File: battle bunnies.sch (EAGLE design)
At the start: 79 parts, among them IC1 CP2104, Q1 mmbt2222, Q2 mmbt2222, SW2 KMR2, U1 PCA9685, U2 SPX3819, U3 MCP73831T-2ACI/OT, X2 ESP-12, X4 20329

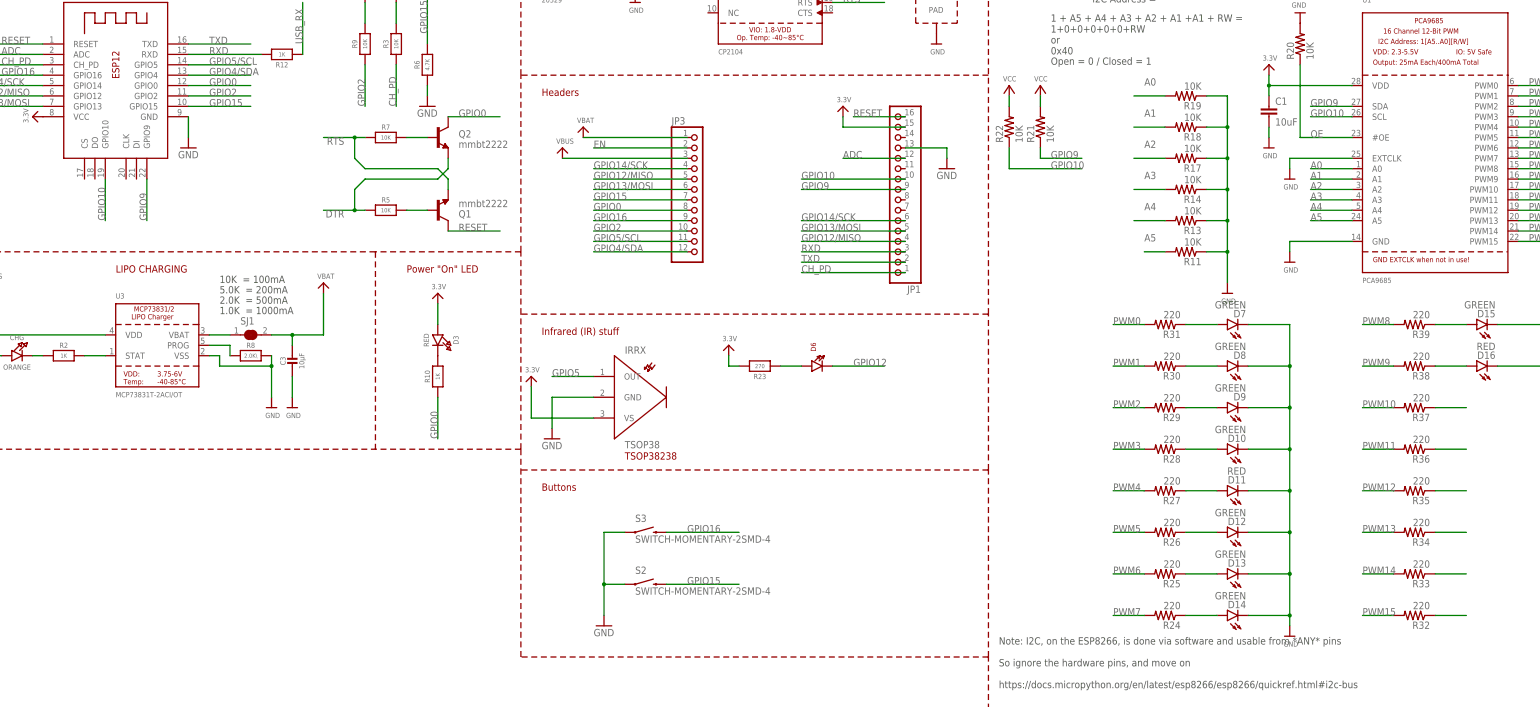
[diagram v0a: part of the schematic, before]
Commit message: Updating schematic, and initial layout
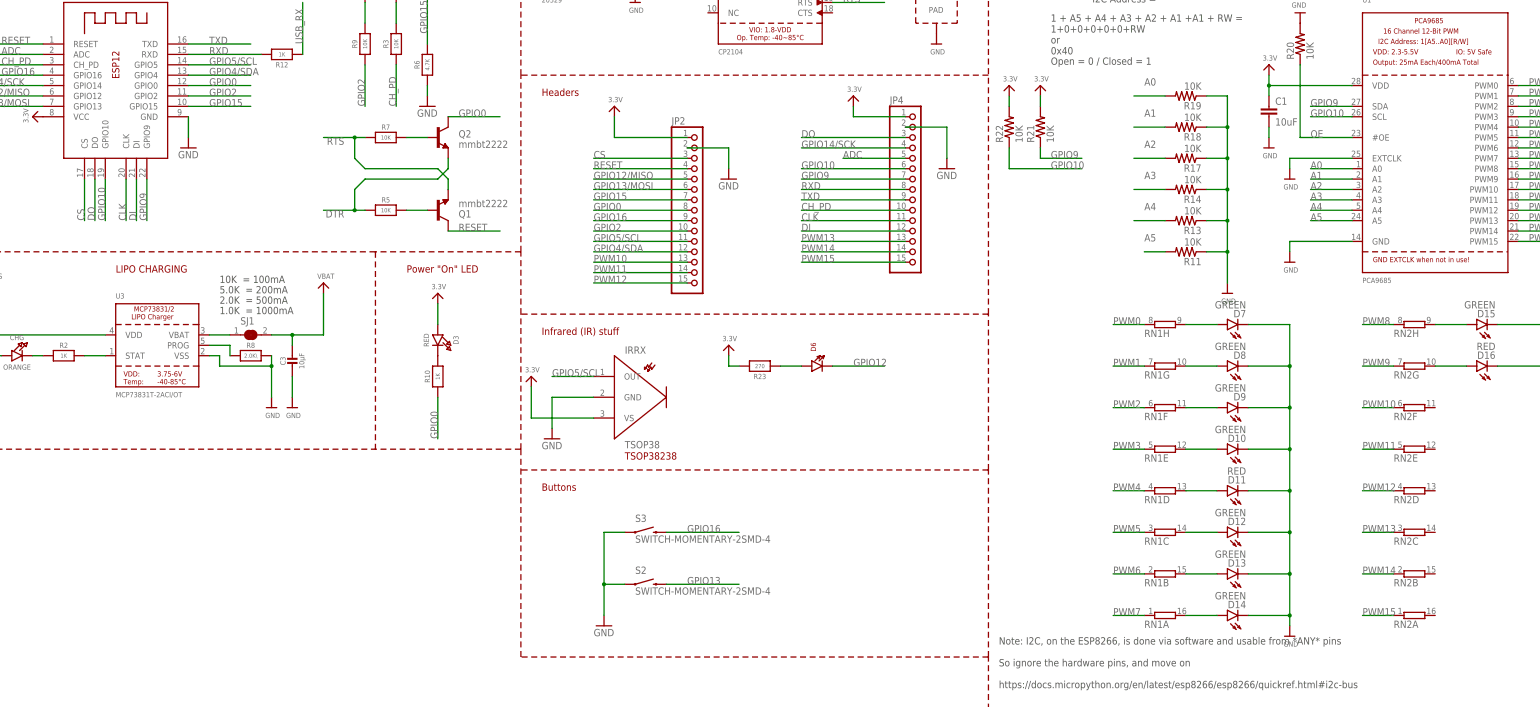
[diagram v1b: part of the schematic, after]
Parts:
- removed JP1: (no value), microbuilder:HEADER-1X16ROUND
- removed JP3: (no value), microbuilder:HEADER-1X12
- removed R24, R25, R26, R27, R28, R29, R30, R31, R32, R33, R34, R35, R36, R37, R38, R39: 220, SparkFun-Passives:RESISTOR0805-RES
- added JP2, JP4: (no value), pinhead:PINHD-1X15
- added RN1, RN2: (no value), resistor-dil:8R-NEXB2HV
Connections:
- removed net GPIO5: IRRX.OUT
- removed net N$25: R37.1
- removed net N$26: R36.1
- removed net N$27: R35.1
- removed net N$28: R34.1
- removed net N$29: R33.1
- removed net N$30: R32.1
- removed net VCC: R21.2, R22.2
- new net CLK: JP4.11, X2.CLK
- new net CS: JP2.3, X2.CS
- new net DI: JP4.12, X2.DI
- new net DO: JP4.3, X2.DO
- new net GPIO13: S2.2
- net 3.3V: now also JP2.1, JP4.1, R21.2, R22.2; no longer JP1.15
- net ADC: now also JP4.5; no longer JP1.12
- net CH_PD: now also JP4.10; no longer JP1.1
- net EN: no longer JP3.2
- net GND: now also JP2.2, JP4.2; no longer JP1.13
- net GPIO0: now also JP2.8; no longer JP3.8
- net GPIO10: now also JP4.6; no longer JP1.10
- net GPIO12/MISO: now also JP2.5; no longer JP1.4, JP3.5
- net GPIO13/MOSI: now also JP2.6; no longer JP1.5, JP3.6
- net GPIO14/SCK: now also JP4.4; no longer JP1.6, JP3.4
- net GPIO15: now also JP2.7; no longer JP3.7, S2.2
- net GPIO16: now also JP2.9; no longer JP3.9
- net GPIO2: now also JP2.10; no longer JP3.10
- net GPIO4/SDA: now also JP2.12; no longer JP3.12
- net GPIO5/SCL: now also IRRX.OUT, JP2.11; no longer JP3.11
- net GPIO9: now also JP4.7; no longer JP1.9
- net N$15: now also RN1B.2; no longer R25.1
- net N$16: now also RN1A.2; no longer R24.1
- net N$17: now also RN1C.2; no longer R26.1
- net N$18: now also RN1D.2; no longer R27.1
- net N$19: now also RN1E.2; no longer R28.1
- net N$20: now also RN1F.2; no longer R29.1
- net N$21: now also RN1G.2; no longer R30.1
- net N$22: now also RN1H.2; no longer R31.1
- net N$23: now also RN2H.2; no longer R39.1
- net N$24: now also RN2G.2; no longer R38.1
- net PWM0: now also RN1H.1; no longer R31.2
- net PWM1: now also RN1G.1; no longer R30.2
- net PWM10: now also JP2.13, RN2F.1; no longer R37.2
- net PWM11: now also JP2.14, RN2E.1; no longer R36.2
- net PWM12: now also JP2.15, RN2D.1; no longer R35.2
- net PWM13: now also JP4.13, RN2C.1; no longer R34.2
- net PWM14: now also JP4.14, RN2B.1; no longer R33.2
- net PWM15: now also JP4.15, RN2A.1; no longer R32.2
- net PWM2: now also RN1F.1; no longer R29.2
- net PWM3: now also RN1E.1; no longer R28.2
- net PWM4: now also RN1D.1; no longer R27.2
- net PWM5: now also RN1C.1; no longer R26.2
- net PWM6: now also RN1B.1; no longer R25.2
- net PWM7: now also RN1A.1; no longer R24.2
- net PWM8: now also RN2H.1; no longer R39.2
- net PWM9: now also RN2G.1; no longer R38.2
- net RESET: now also JP2.4; no longer JP1.16
- net RXD: now also JP4.8; no longer JP1.3
- net TXD: now also JP4.9; no longer JP1.2
- net VBAT: no longer JP3.1
- net VBUS: no longer JP3.3

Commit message: Updating with latest routing attempt
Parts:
- removed R11, R13, R14, R17, R18, R19: 10K, SparkFun-Passives:RESISTOR0805-RES
- added RN3: (no value), resistor-dil:8R-NEXB2HV
- RN1: value (none) -> 220
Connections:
- removed net GPIO13: S2.2
- net A0: now also RN3E.1; no longer R19.2
- net A1: now also RN3D.1; no longer R18.2
- net A2: now also RN3C.1; no longer R17.2
- net A3: now also RN3B.1; no longer R14.2
- net A4: now also RN3A.1; no longer R13.2
- net A5: now also RN3F.1; no longer R11.2
- net GND: now also RN3A.2, RN3B.2, RN3C.2, RN3D.2, RN3E.2, RN3F.2; no longer R11.1, R13.1, R14.1, R17.1, R18.1, R19.1
- net GPIO13/MOSI: now also S2.2
- net PWM10: no longer RN2F.1
- net PWM11: no longer RN2E.1
- net PWM12: no longer RN2D.1
- net PWM13: no longer RN2C.1
- net PWM14: no longer RN2B.1
- net PWM15: no longer RN2A.1
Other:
- moved on the sheet: RN2A, RN2B, RN2C, RN2D, RN2E, RN2F
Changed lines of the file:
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@@
 <?xml version="1.0" encoding="utf-8"?>
 <!DOCTYPE eagle SYSTEM "eagle.dtd">
-<eagle version="7.7.0">
+<eagle version="7.6.0">
 <drawing>
 <settings>
@@
 <part name="U$63" library="microbuilder" deviceset="GND" device=""/>
 <part name="U$69" library="microbuilder" deviceset="GND" device=""/>
-<part name="R11" library="SparkFun-Passives" deviceset="RESISTOR" device="0805-RES" value="10K"/>
-<part name="R13" library="SparkFun-Passives" deviceset="RESISTOR" device="0805-RES" value="10K"/>
-<part name="R14" library="SparkFun-Passives" deviceset="RESISTOR" device="0805-RES" value="10K"/>
-<part name="R17" library="SparkFun-Passives" deviceset="RESISTOR" device="0805-RES" value="10K"/>
-<part name="R18" library="SparkFun-Passives" deviceset="RESISTOR" device="0805-RES" value="10K"/>
-<part name="R19" library="SparkFun-Passives" deviceset="RESISTOR" device="0805-RES" value="10K"/>
 <part name="U$70" library="microbuilder" deviceset="GND" device=""/>
 <part name="C1" library="SparkFun-Capacitors" deviceset="10UF10V10%(0805)" device="" value="10uF"/>
@@
 <part name="U$35" library="microbuilder" deviceset="3.3V" device=""/>
 <part name="GND7" library="supply1" deviceset="GND" device=""/>
+<part name="RN1" library="resistor-dil" deviceset="8R-N" device="EXB2HV" value="220"/>
 <part name="RN2" library="resistor-dil" deviceset="8R-N" device="EXB2HV"/>
-<part name="RN1" library="resistor-dil" deviceset="8R-N" device="EXB2HV"/>
+<part name="RN3" library="resistor-dil" deviceset="8R-N" device="EXB2HV"/>
 </parts>
 <sheets>
@@
 <instance part="U$63" gate="G$1" x="325.12" y="142.24"/>
 <instance part="U$69" gate="G$1" x="309.88" y="134.62"/>
-<instance part="R11" gate="G$1" x="299.72" y="144.78" rot="R180"/>
-<instance part="R13" gate="G$1" x="299.72" y="152.4" rot="R180"/>
-<instance part="R14" gate="G$1" x="299.72" y="160.02" rot="R180"/>
-<instance part="R17" gate="G$1" x="299.72" y="167.64" rot="R180"/>
-<instance part="R18" gate="G$1" x="299.72" y="175.26" rot="R180"/>
-<instance part="R19" gate="G$1" x="299.72" y="182.88" rot="R180"/>
 <instance part="U$70" gate="G$1" x="320.04" y="170.18"/>
 <instance part="C1" gate="G$1" x="320.04" y="177.8"/>
@@
 <instance part="U$35" gate="G$1" x="160.02" y="180.34"/>
 <instance part="GND7" gate="1" x="187.96" y="162.56"/>
-<instance part="RN2" gate="A" x="355.6" y="55.88"/>
-<instance part="RN2" gate="B" x="355.6" y="66.04"/>
-<instance part="RN2" gate="C" x="355.6" y="76.2"/>
-<instance part="RN2" gate="D" x="355.6" y="86.36"/>
-<instance part="RN2" gate="E" x="355.6" y="96.52"/>
-<instance part="RN2" gate="F" x="355.6" y="106.68"/>
-<instance part="RN2" gate="G" x="355.6" y="116.84"/>
-<instance part="RN2" gate="H" x="355.6" y="127"/>
 <instance part="RN1" gate="A" x="294.64" y="55.88"/>
 <instance part="RN1" gate="B" x="294.64" y="66.04"/>
@@
 <instance part="RN1" gate="G" x="294.64" y="116.84"/>
 <instance part="RN1" gate="H" x="294.64" y="127"/>
+<instance part="RN2" gate="A" x="368.3" y="104.14"/>
+<instance part="RN2" gate="B" x="368.3" y="99.06"/>
+<instance part="RN2" gate="C" x="368.3" y="93.98"/>
+<instance part="RN2" gate="D" x="368.3" y="88.9"/>
+<instance part="RN2" gate="E" x="368.3" y="83.82"/>
+<instance part="RN2" gate="F" x="368.3" y="78.74"/>
+<instance part="RN2" gate="G" x="355.6" y="116.84"/>
+<instance part="RN2" gate="H" x="355.6" y="127"/>
+<instance part="RN3" gate="A" x="299.72" y="152.4"/>
+<instance part="RN3" gate="B" x="299.72" y="160.02"/>
+<instance part="RN3" gate="C" x="299.72" y="167.64"/>
+<instance part="RN3" gate="D" x="299.72" y="175.26"/>
+<instance part="RN3" gate="E" x="299.72" y="182.88"/>
+<instance part="RN3" gate="F" x="299.72" y="144.78"/>
+<instance part="RN3" gate="G" x="264.16" y="124.46"/>
+<instance part="RN3" gate="H" x="264.16" y="119.38"/>
 </instances>
 <busses>
@@
 <wire x1="304.8" y1="182.88" x2="309.88" y2="182.88" width="0.1524" layer="91"/>
 <wire x1="309.88" y1="182.88" x2="309.88" y2="175.26" width="0.1524" layer="91"/>
-<pinref part="R19" gate="G$1" pin="1"/>
 <pinref part="U$69" gate="G$1" pin="GND"/>
-<pinref part="R18" gate="G$1" pin="1"/>
 <wire x1="309.88" y1="175.26" x2="309.88" y2="167.64" width="0.1524" layer="91"/>
 <wire x1="309.88" y1="167.64" x2="309.88" y2="160.02" width="0.1524" layer="91"/>
@@
 <wire x1="304.8" y1="175.26" x2="309.88" y2="175.26" width="0.1524" layer="91"/>
 <junction x="309.88" y="175.26"/>
-<pinref part="R17" gate="G$1" pin="1"/>
 <wire x1="304.8" y1="167.64" x2="309.88" y2="167.64" width="0.1524" layer="91"/>
 <junction x="309.88" y="167.64"/>
-<pinref part="R14" gate="G$1" pin="1"/>
 <wire x1="304.8" y1="160.02" x2="309.88" y2="160.02" width="0.1524" layer="91"/>
 <junction x="309.88" y="160.02"/>
-<pinref part="R13" gate="G$1" pin="1"/>
 <wire x1="304.8" y1="152.4" x2="309.88" y2="152.4" width="0.1524" layer="91"/>
 <junction x="309.88" y="152.4"/>
-<pinref part="R11" gate="G$1" pin="1"/>
 <wire x1="304.8" y1="144.78" x2="309.88" y2="144.78" width="0.1524" layer="91"/>
 <junction x="309.88" y="144.78"/>
+<pinref part="RN3" gate="F" pin="2"/>
+<pinref part="RN3" gate="A" pin="2"/>
+<pinref part="RN3" gate="B" pin="2"/>
+<pinref part="RN3" gate="C" pin="2"/>
+<pinref part="RN3" gate="D" pin="2"/>
+<pinref part="RN3" gate="E" pin="2"/>
 </segment>
 <segment>
@@
 <pinref part="JP2" gate="A" pin="6"/>
 </segment>
+<segment>
+<wire x1="172.72" y1="63.5" x2="190.5" y2="63.5" width="0.1524" layer="91"/>
+<label x="177.8" y="63.5" size="1.778" layer="95"/>
+<pinref part="S2" gate="G$1" pin="2"/>
+</segment>
 </net>
 <net name="GPIO12/MISO" class="0">
@@
 <wire x1="350.52" y1="106.68" x2="342.9" y2="106.68" width="0.1524" layer="91"/>
 <label x="342.9" y="106.68" size="1.778" layer="95"/>
-<pinref part="RN2" gate="F" pin="1"/>
 </segment>
 <segment>
@@
 <wire x1="350.52" y1="96.52" x2="342.9" y2="96.52" width="0.1524" layer="91"/>
 <label x="342.9" y="96.52" size="1.778" layer="95"/>
-<pinref part="RN2" gate="E" pin="1"/>
 </segment>
 <segment>
@@
 <wire x1="350.52" y1="86.36" x2="342.9" y2="86.36" width="0.1524" layer="91"/>
 <label x="342.9" y="86.36" size="1.778" layer="95"/>
-<pinref part="RN2" gate="D" pin="1"/>
 </segment>
 <segment>
@@
 <wire x1="350.52" y1="76.2" x2="342.9" y2="76.2" width="0.1524" layer="91"/>
 <label x="342.9" y="76.2" size="1.778" layer="95"/>
-<pinref part="RN2" gate="C" pin="1"/>
 </segment>
 <segment>
@@
 <wire x1="350.52" y1="66.04" x2="342.9" y2="66.04" width="0.1524" layer="91"/>
 <label x="342.9" y="66.04" size="1.778" layer="95"/>
-<pinref part="RN2" gate="B" pin="1"/>
 </segment>
 <segment>
@@
 <wire x1="350.52" y1="55.88" x2="342.9" y2="55.88" width="0.1524" layer="91"/>
 <label x="342.9" y="55.88" size="1.778" layer="95"/>
-<pinref part="RN2" gate="A" pin="1"/>
 </segment>
 <segment>
@@
 <wire x1="287.02" y1="182.88" x2="294.64" y2="182.88" width="0.1524" layer="91"/>
 <label x="289.56" y="185.42" size="1.778" layer="95"/>
-<pinref part="R19" gate="G$1" pin="2"/>
+<pinref part="RN3" gate="E" pin="1"/>
 </segment>
 </net>
@@
 <wire x1="287.02" y1="175.26" x2="294.64" y2="175.26" width="0.1524" layer="91"/>
 <label x="289.56" y="177.8" size="1.778" layer="95"/>
-<pinref part="R18" gate="G$1" pin="2"/>
+<pinref part="RN3" gate="D" pin="1"/>
 </segment>
 </net>
@@
 <wire x1="287.02" y1="167.64" x2="294.64" y2="167.64" width="0.1524" layer="91"/>
 <label x="289.56" y="170.18" size="1.778" layer="95"/>
-<pinref part="R17" gate="G$1" pin="2"/>
+<pinref part="RN3" gate="C" pin="1"/>
 </segment>
 </net>
@@
 <wire x1="287.02" y1="160.02" x2="294.64" y2="160.02" width="0.1524" layer="91"/>
 <label x="289.56" y="162.56" size="1.778" layer="95"/>
-<pinref part="R14" gate="G$1" pin="2"/>
+<pinref part="RN3" gate="B" pin="1"/>
 </segment>
 </net>
@@
 <wire x1="287.02" y1="152.4" x2="294.64" y2="152.4" width="0.1524" layer="91"/>
 <label x="289.56" y="154.94" size="1.778" layer="95"/>
-<pinref part="R13" gate="G$1" pin="2"/>
+<pinref part="RN3" gate="A" pin="1"/>
 </segment>
 </net>
@@
 <wire x1="289.56" y1="144.78" x2="294.64" y2="144.78" width="0.1524" layer="91"/>
 <label x="289.56" y="147.32" size="1.778" layer="95"/>
-<pinref part="R11" gate="G$1" pin="2"/>
+<pinref part="RN3" gate="F" pin="1"/>
 </segment>
 </net>
@@
 </segment>
 </net>
-<net name="GPIO13" class="0">
-<segment>
-<wire x1="172.72" y1="63.5" x2="190.5" y2="63.5" width="0.1524" layer="91"/>
-<label x="177.8" y="63.5" size="1.778" layer="95"/>
-<pinref part="S2" gate="G$1" pin="2"/>
-</segment>
-</net>
